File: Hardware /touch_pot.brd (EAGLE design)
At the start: 44.5 x 78.7 mm, 73 parts, among them CON1 SINGLE_PADSMD, CON10 SINGLE_PADSMD, CON11 SINGLE_PADSMD, CON12 SINGLE_PADSMD, CON13 SINGLE_PADSMD, CON14 SINGLE_PADSMD, CON15 SINGLE_PADSMD, CON16 SINGLE_PADSMD_R, CON17 SINGLE_PADSMD_R, CON18 SINGLE_PADSMD_R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

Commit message: First Round of changes before Protos
Changed Dimension thickness
Changed silk ratio
Added designed by name
Bumped via size up to 0.020
Added actual stand-offs instead of drill hits
Labeled push button
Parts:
- added STANDOFF1, STANDOFF2: STAND-OFFTIGHT, SparkFun-Electromechanical:STAND-OFF-TIGHT
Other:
- board text added: "Address"
- board text added: "I2C"
- board text added: "V10"
- board text removed: "Rev 1"

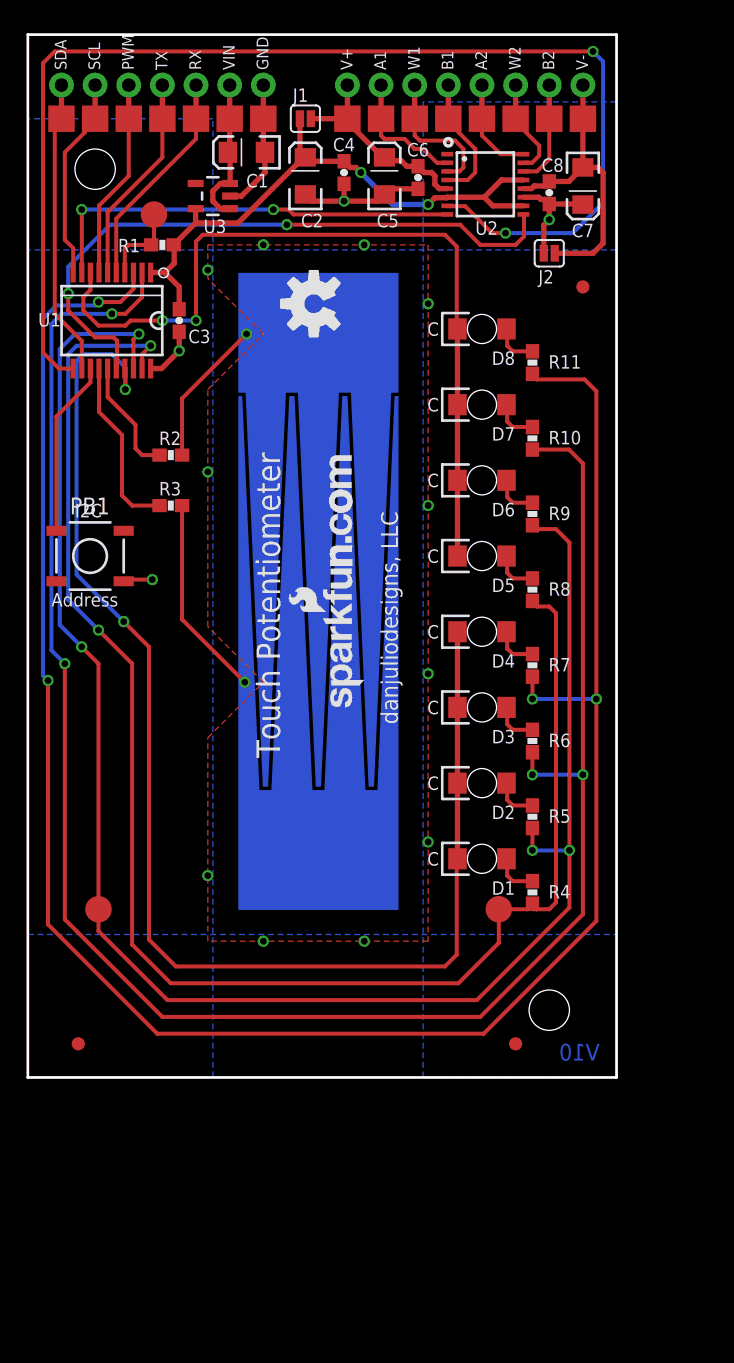
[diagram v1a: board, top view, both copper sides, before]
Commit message: Work in progress
rerouting for fourth standoff hole
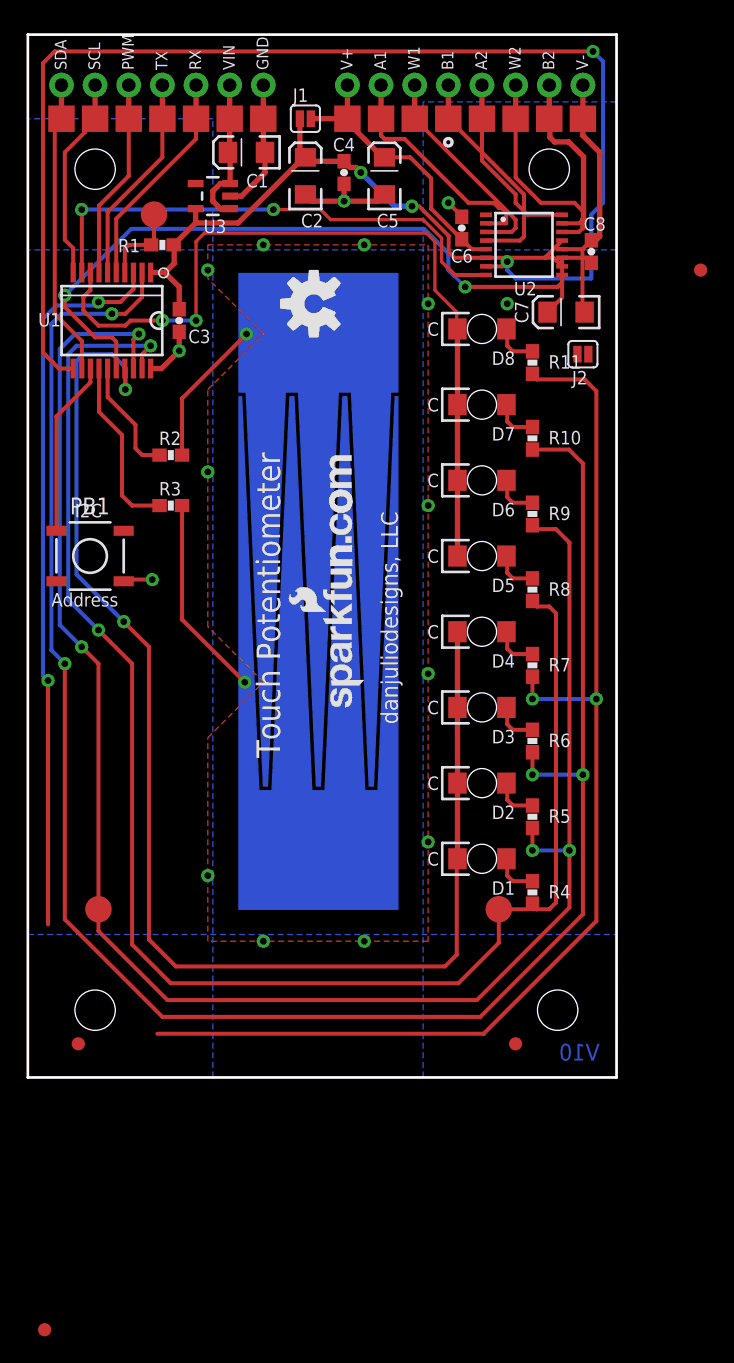
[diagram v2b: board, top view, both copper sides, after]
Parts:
- added STANDOFF3, STANDOFF4: STAND-OFFTIGHT, SparkFun-Electromechanical:STAND-OFF-TIGHT
- added U$5: FIDUCIAL, djd_eagle_library:FIDUCIAL
- moved STANDOFF1 63.5 mm to (39.4, 68.6)
- moved C7 9.61 mm to (40.6, 57.8), turned to 180 degrees
- moved U$2 8.98 mm to (50.8, 61.0)
- moved J2 8.03 mm to (41.9, 54.6)
- moved C8 5.46 mm to (42.5, 62.4)
- moved U2 5.43 mm to (37.5, 62.9)
- moved C6 5.04 mm to (32.8, 64.1), turned to 90 degrees
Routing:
- net LA3: track 155.2 -> 143.5 mm
- net A1: track 9.66 -> 18.0 mm
- net W2: track 7.48 -> 15.4 mm
- net B1: track 9.79 -> 16.8 mm
- net A2: track 7.52 -> 13.8 mm
- net B2: track 7.92 -> 14.2 mm
- net SDO: track 32.5 -> 38.4 mm
- net V+: track 16.4 -> 22.2 mm
- net W1: track 10.7 -> 16.3 mm
- net +5V: track 45.5 -> 48.9 mm
- net CSN: track 48.4 -> 50.8 mm
- net V-: track 22.4 -> 20.0 mm
- net GND: track 36.3 -> 33.9 mm, vias 15 -> 16
- net SCLK: track 91.8 -> 93.4 mm
- net LED_PWM2: track 61.8 -> 61.2 mm

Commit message: Last commit before protos
Finally rerouted to add space for fourth stand-off hole.
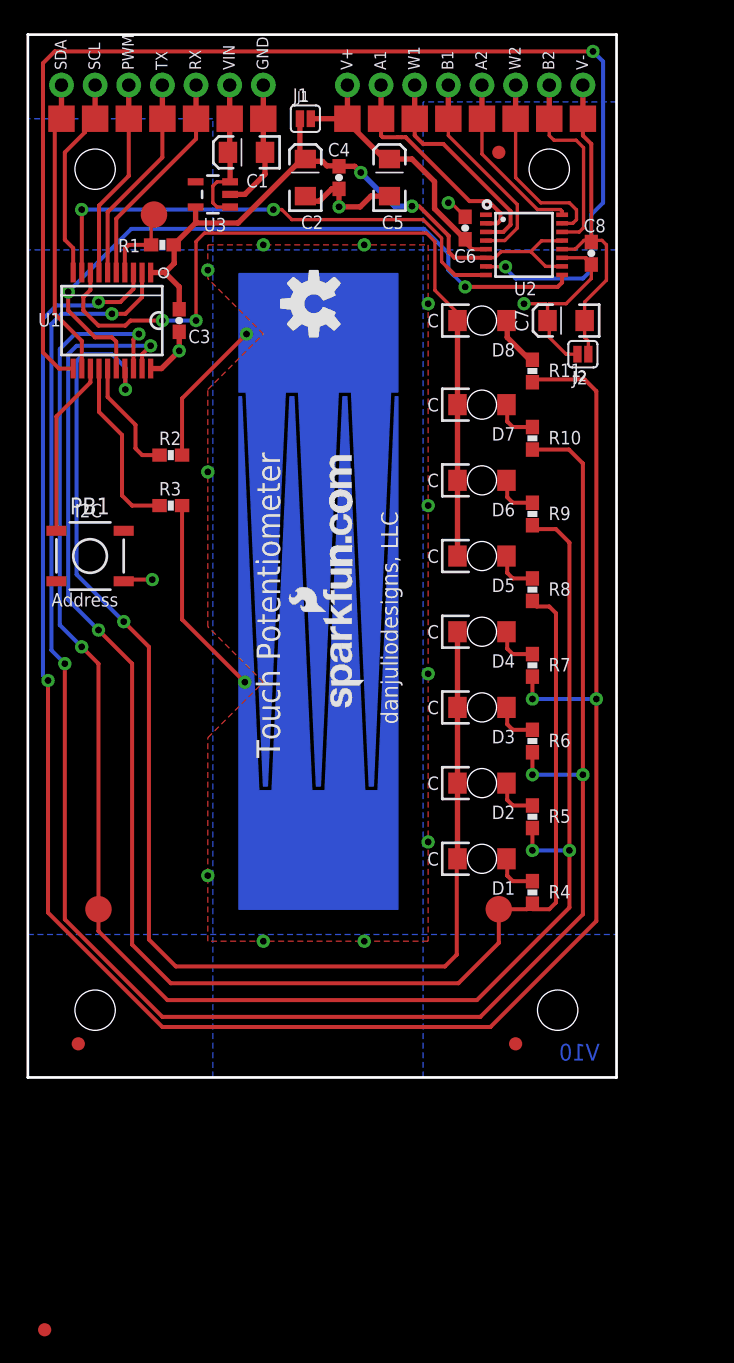
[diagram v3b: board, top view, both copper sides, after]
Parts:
- moved U$2 17.6 mm to (35.6, 69.8)
- moved C7 0.63 mm to (40.6, 57.1)
- moved D8 0.63 mm to (34.3, 57.1)
- moved R11 0.63 mm to (38.1, 53.3)
- moved C4 0.54 mm to (23.5, 67.9)
- moved C5 0.40 mm to (27.3, 67.9)
- moved C6 0.25 mm to (33.0, 64.1)
- moved C2 0.13 mm to (21.0, 67.9)
- moved C8 0.13 mm to (42.5, 62.2)
- moved U3 0.13 mm to (14.0, 66.7)
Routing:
- net LA3: track 143.5 -> 154.1 mm
- net GND: track 33.9 -> 42.2 mm
- net V-: track 20.0 -> 25.0 mm
- net +5V: track 48.9 -> 50.7 mm
- net LED_PWM2: track 61.2 -> 62.4 mm
- net B1: track 16.8 -> 15.7 mm
- net A1: track 18.0 -> 17.0 mm
- net SCLK: track 93.4 -> 92.4 mm
- net W2: track 15.4 -> 14.5 mm
- net N$8: track 3.37 -> 3.90 mm
- net A2: track 13.8 -> 13.3 mm
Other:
- board text added: "J1"
- board text added: "J2"
